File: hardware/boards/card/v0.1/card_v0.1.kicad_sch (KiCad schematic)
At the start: 72 parts, among them IC1 IS42S16160J-7BLI, IC2 IS42S16160J-7BLI, J1 SODIMM-200, J2 USB_HOST, J3 USB_DEVICE, J4 SD_CARD, J5 DEBUG, J6 SPI, J7 UART4, J8 Conn_01x16_Pin, J9 AUDIO_IN, U1 CS42528K-CQZ, U2 STM32H747XIHx, U3 NJM4580E-TE1, U4 NJM4580E-TE1, Y1 Crystal, Y2 Crystal

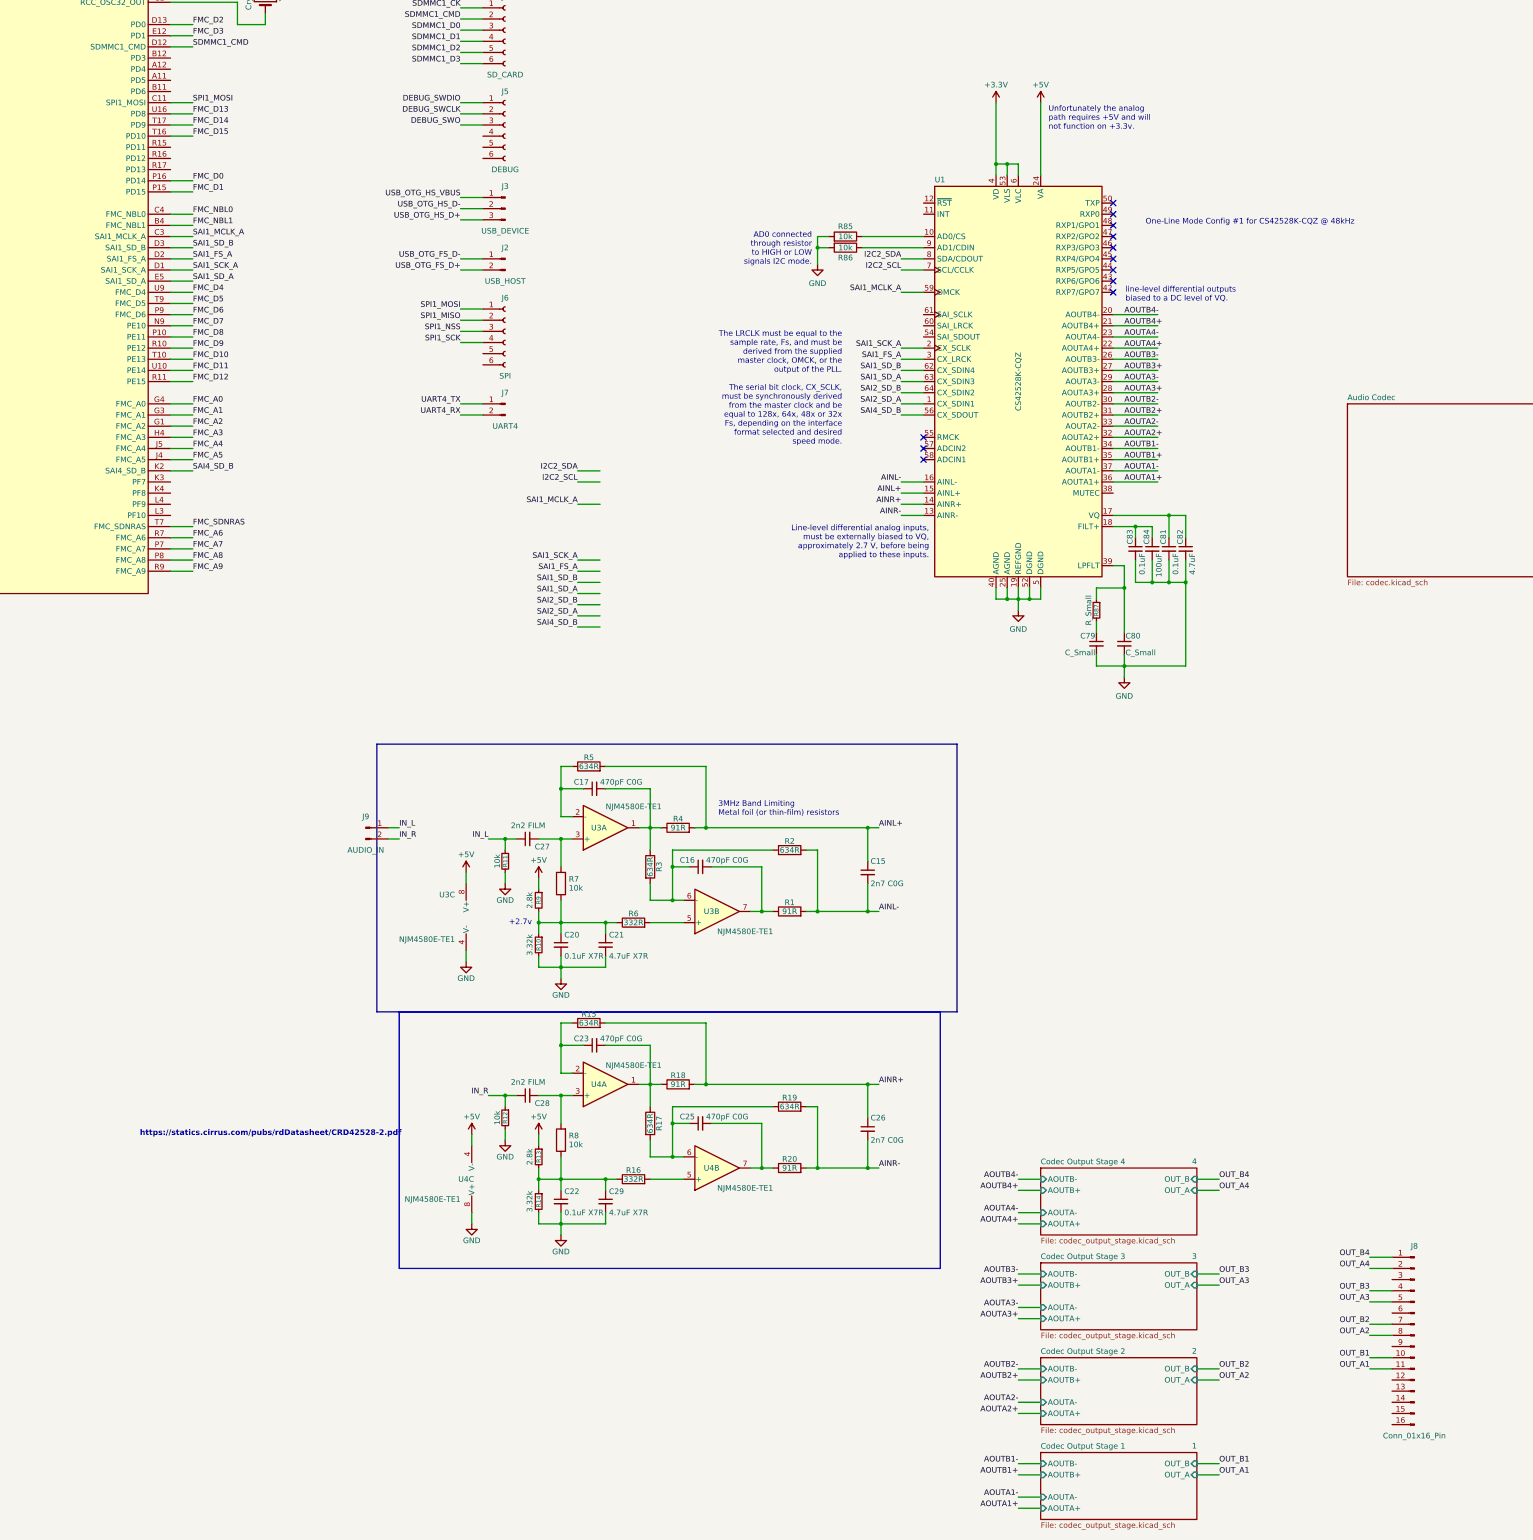
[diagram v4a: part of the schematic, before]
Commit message: card: add filter caps for codec
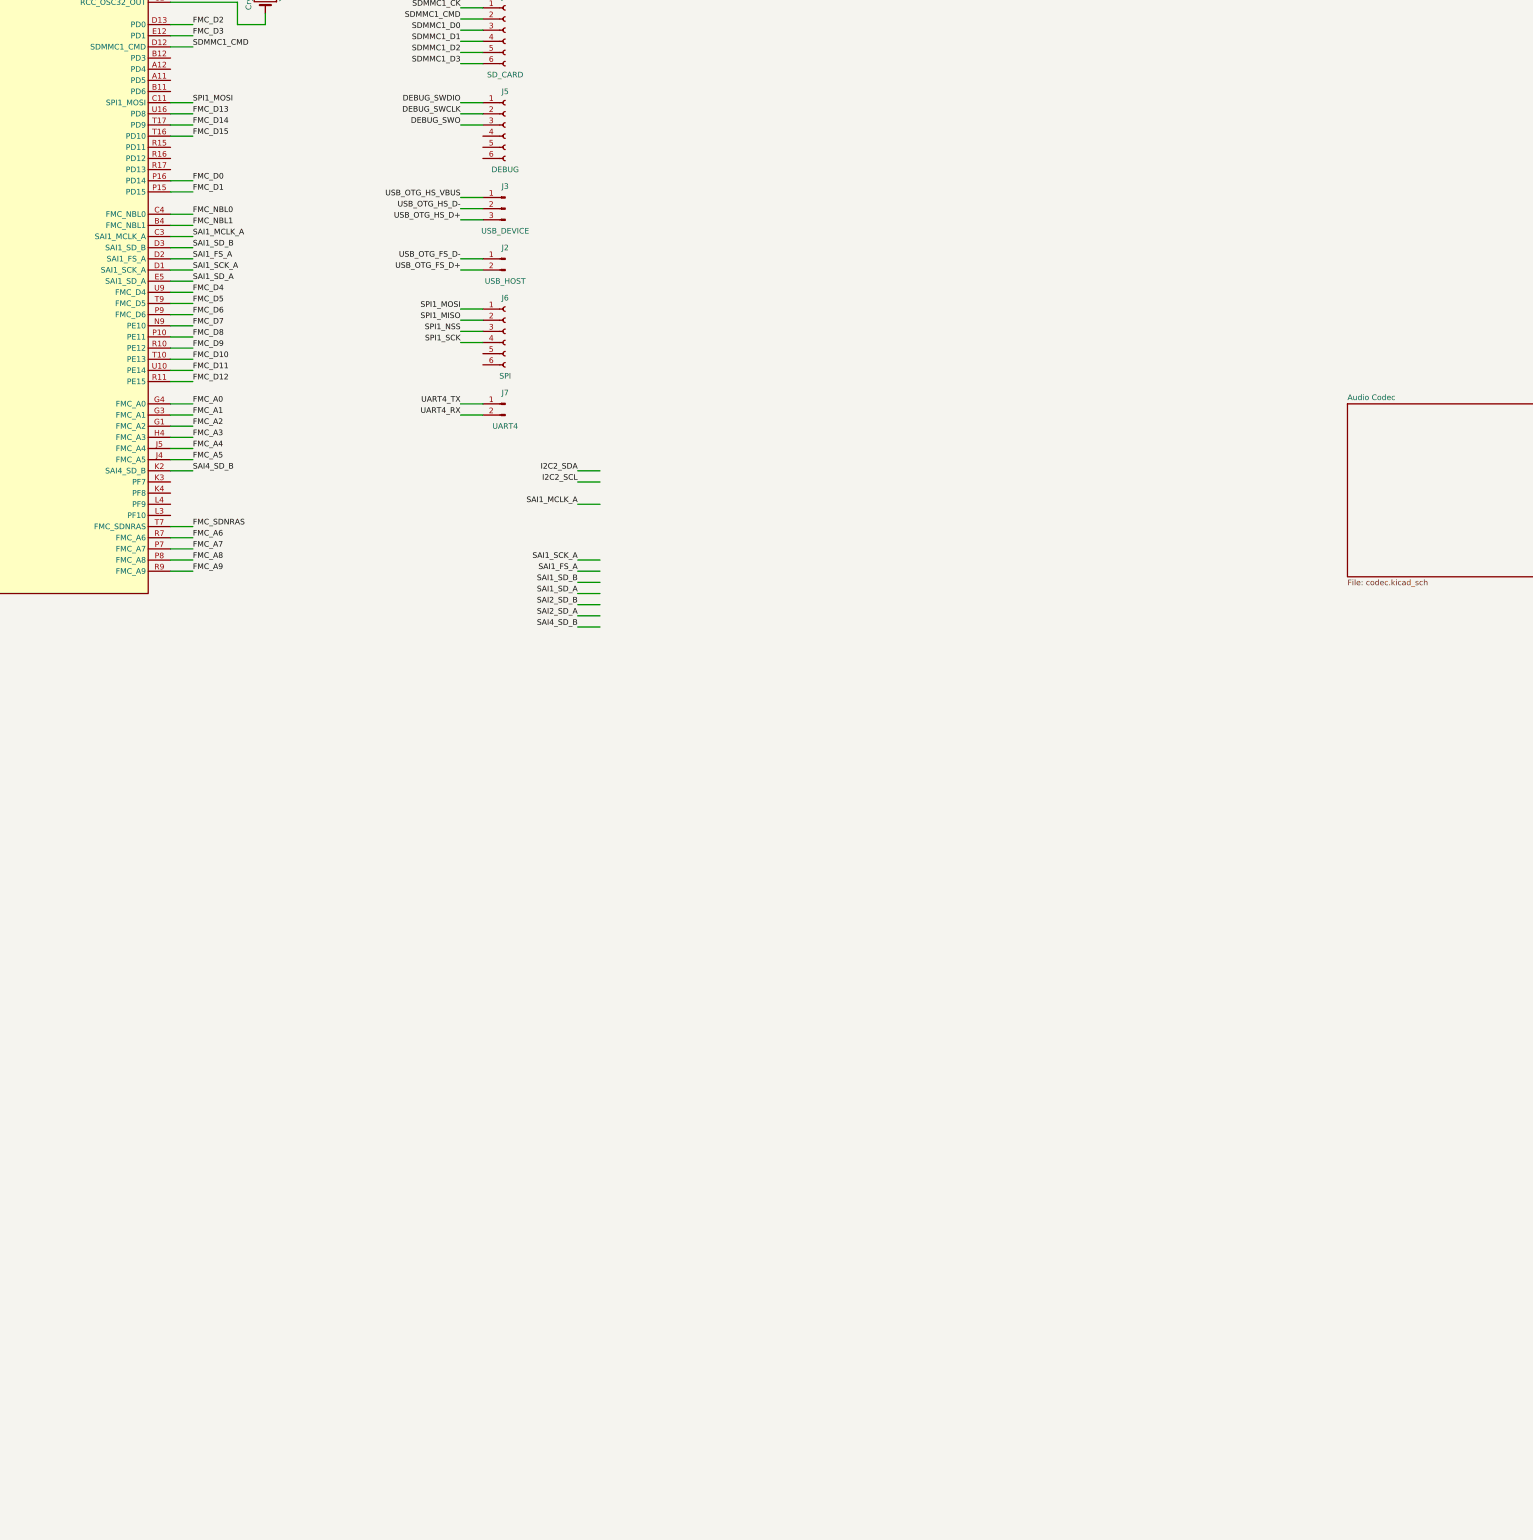
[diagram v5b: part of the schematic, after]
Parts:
- removed C15, C26: 2n7 C0G, rhais_rcl.pretty-main:C0402, symbol Device:C_Small
- removed C16, C17, C23, C25: 470pF C0G, rhais_rcl.pretty-main:C0402, symbol Device:C_Small
- removed C20, C22: 0.1uF X7R, rhais_rcl.pretty-main:C0402, symbol Device:C_Small
- removed C21, C29: 4.7uF X7R, rhais_rcl.pretty-main:C0402, symbol Device:C_Small
- removed C27, C28: 2n2 FILM, rhais_rcl.pretty-main:C0603, symbol Device:C_Small
- removed C79, C80: C_Small, symbol Device:C_Small
- removed C81, C83: 0.1uF, rhais_rcl.pretty-main:C0402, symbol Device:C_Small
- removed C82: 4.7uF, rhais_rcl.pretty-main:C0402, symbol Device:C_Small
- removed C84: 100uF, rhais_rcl.pretty-main:C0402, symbol Device:C_Small
- removed J8: Conn_01x16_Pin, Connector_PinHeader_1.27mm:PinHeader_1x16_P1.27mm_Vertical, symbol Connector:Conn_01x16_Pin
- removed J9: AUDIO_IN, Connector_PinHeader_1.27mm:PinHeader_1x02_P1.27mm_Vertical, symbol Connector:Conn_01x02_Pin
- removed R1, R18, R20, R4: 91R, rhais_rcl.pretty-main:R0402, symbol Device:R
- removed R10, R14: 3.32k, rhais_rcl.pretty-main:R0402, symbol Device:R_Small
- removed R11, R12: 10k, rhais_rcl.pretty-main:R0402, symbol Device:R_Small
- removed R13, R9: 2.8k, rhais_rcl.pretty-main:R0402, symbol Device:R_Small
- removed R15, R17, R19, R2, R3, R5: 634R, rhais_rcl.pretty-main:R0402, symbol Device:R
- removed R16, R6: 332R, rhais_rcl.pretty-main:R0402, symbol Device:R
- removed R7, R8, R85, R86: 10k, rhais_rcl.pretty-main:R0402, symbol Device:R
- removed R87: R_Small, symbol Device:R_Small
- removed U1: CS42528K-CQZ, Package_QFP:LQFP-64_10x10mm_P0.5mm, symbol Northernpaws_Audio:CS42528K-CQZ
- removed U3, U4: NJM4580E-TE1, Package_SO:TSSOP-8_3x3mm_P0.65mm, symbol Amplifier_Operational:NJM4580
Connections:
- no-connect marks 12 -> 0
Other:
- removed sheet Codec Output Stage 1
- removed sheet Codec Output Stage 2
- removed sheet Codec Output Stage 3
- removed sheet Codec Output Stage 4
- note removed: "+2.7v"
- note removed: "3MHz Band Limiting Metal foil (or thin-film) resistors"
- note removed: "AD0 connected through resistor to HIGH or LOW signals I2C mode."
- note removed: "Line-level differential analog inputs, must be externally biased to VQ, approximately 2.7 V, before being applied to these inputs."
- note removed: "One-Line Mode Config #1 for CS42528K-CQZ @ 48kHz"
- note removed: "The LRCLK must be equal to the sample rate, Fs, and must be derived from the supplied master clock, OMCK, or the output of the PLL. The serial bit clock, CX_SCLK, must be synchronously derived from the master clock and be equal to 128x, 64x, 48x or 32x Fs, depending on the interface format selected and desired speed mode."
- note removed: "Unfortunately the analog path requires +5V and will not function on +3.3v."
- note removed: "https://statics.cirrus.com/pubs/rdDatasheet/CRD42528-2.pdf"
- note removed: "line-level differential outputs biased to a DC level of VQ."
